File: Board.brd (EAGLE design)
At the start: 55.9 x 46.7 mm, 29 parts, among them Q1 N-MOS-FET, Q2 N-MOS-FET, Q3 N-MOS-FET, U2 STM32F07

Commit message: rev 2 preliminary, added power LED, power switch, necessary MCU pullups/downs and fets for the RGB
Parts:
- removed BARREL1: (no value), pinhead:1X02
- added PWR-SWITCH: (no value), pinhead:1X02
- C2: value 10uF -> 47uF; device rcl:C0805 -> rcl:C0603
- C3, C4: device rcl:C0805 -> rcl:C0603
- R1, R2, R3, R4, R5: device rcl:R0805 -> rcl:R0603
- R11, R12, R9: value 250 -> 250r; device rcl:R0805 -> rcl:R0603
- R6: value 250 -> 200; device rcl:R0805 -> rcl:R0603
- R7: value 300 -> 200; device rcl:R0805 -> rcl:R0603
- moved SWITCH 7.62 mm to (3.81, 29.2)
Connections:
- net N$1: now also PWR-SWITCH.2; no longer SWITCH.2
- net VBAT: now also SWITCH.2; no longer BARREL1.2
- net VIN: now also PWR-SWITCH.1; no longer BARREL1.1
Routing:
- net GND: vias 42 -> 43
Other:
- board text added: "B"
- board text added: "Designed By Michael Yablonovitch May 8 2018"
- board text added: "G"
- board text added: "MFLB Power Adapter - Rev.2"
- board text added: "R"
- board text removed: "MFLB Power Adapter - Rev.2 Designed By Michael Yablonovitch May 8 2018"

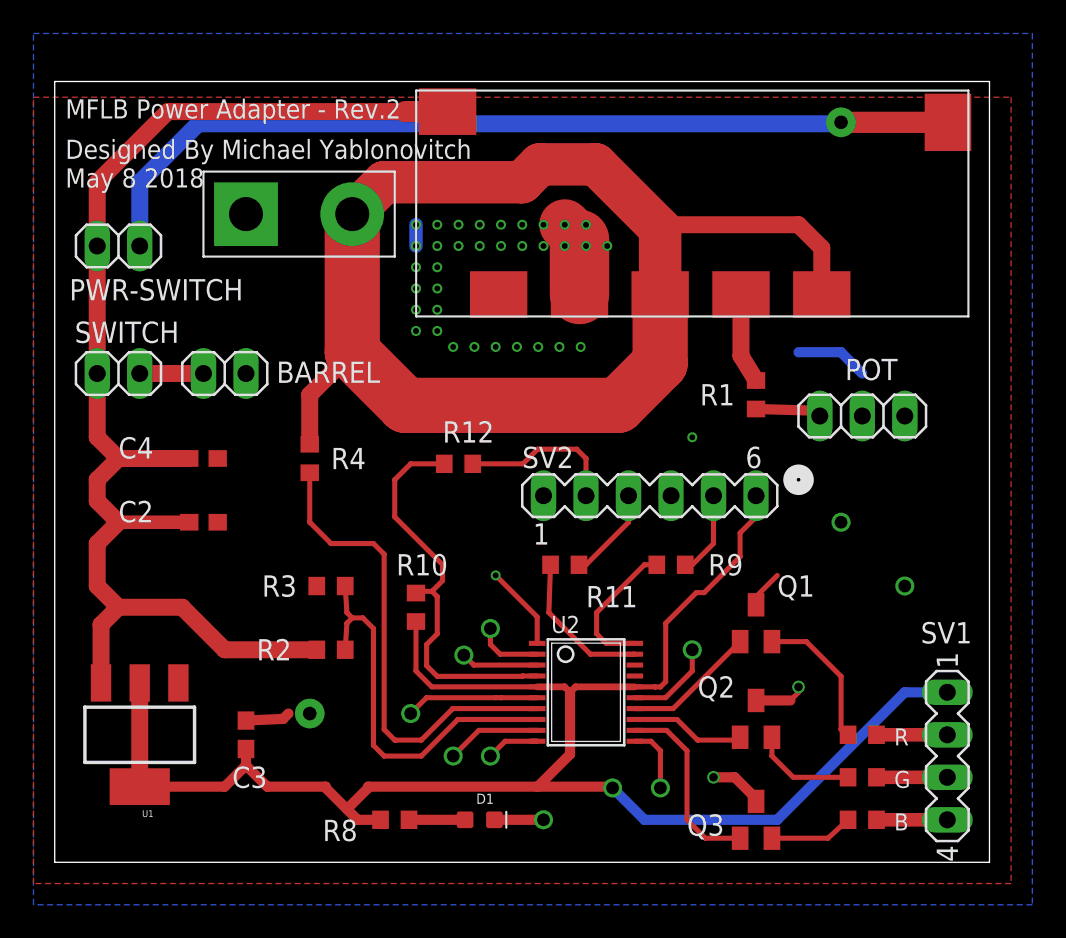
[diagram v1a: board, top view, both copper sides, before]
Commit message: switched n-mos to p-mos for common cathode RGBs
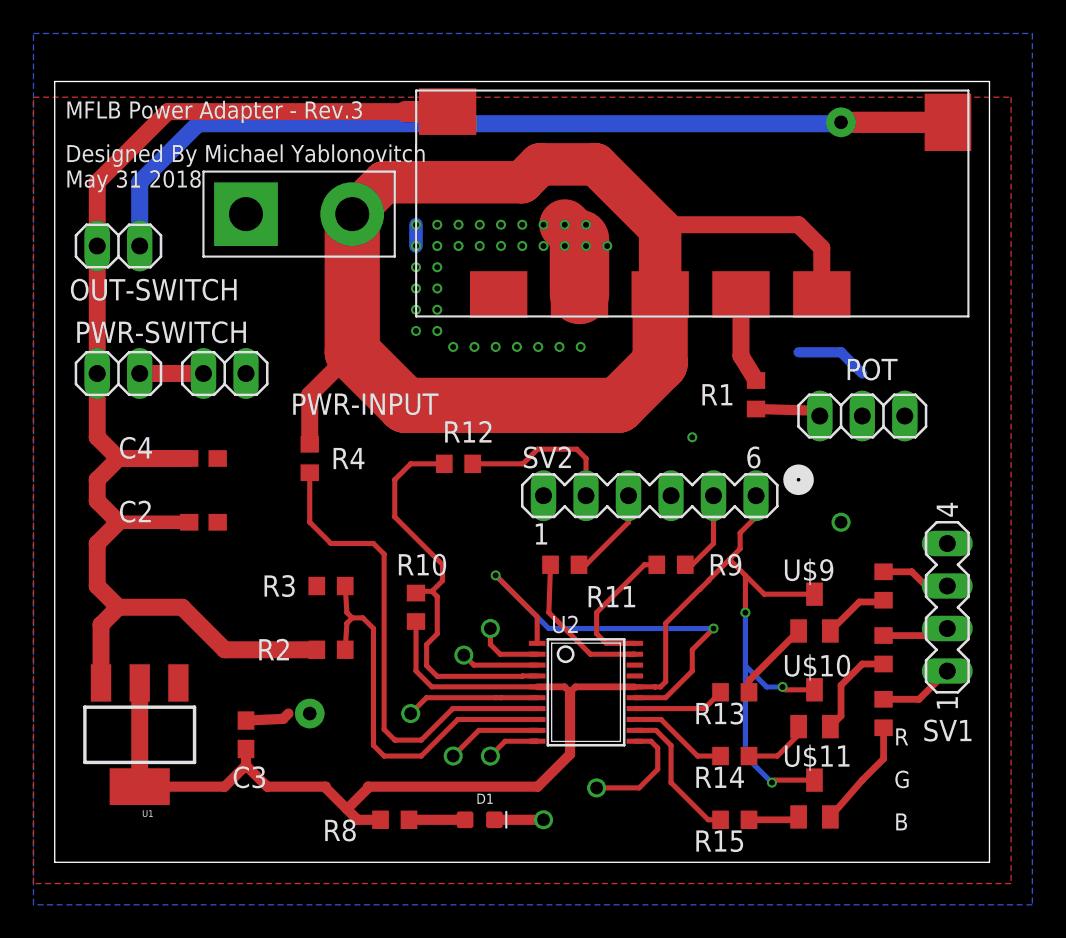
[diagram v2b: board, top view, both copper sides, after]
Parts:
- removed Q1, Q2, Q3: N-MOS-FET, YabzLib:SOT23
- removed SWITCH: (no value), pinhead:1X02
- added OUT-SWITCH: (no value), pinhead:1X02
- added R13, R14, R15: 250, rcl:R0603
- added U$10, U$11, U$9: P-MOS-FET, YabzLib:SOT23
- moved R5 8.98 mm to (49.5, 16.5), turned to 90 degrees
- moved SV1 8.89 mm to (53.3, 15.2), turned to 90 degrees
- moved R6 7.73 mm to (49.5, 12.7), turned to 90 degrees
- moved PWR-SWITCH 7.62 mm to (3.81, 29.2)
- moved R7 6.48 mm to (49.5, 8.89), turned to 90 degrees
- renumbered BARREL to PWR-INPUT
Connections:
- new net N$6: R7.2, SV1.1
- new net N$7: R13.1, U$9.B
- new net N$8: R14.1, U$10.B
- net +3V3: now also U$10.E, U$11.E, U$9.E; no longer SV1.1
- net GND: now also SV1.4; no longer Q1.E, Q2.E, Q3.E
- net LED-B: now also R15.2; no longer Q3.B
- net LED-G: now also R14.2; no longer Q2.B
- net LED-R: now also R13.2; no longer Q1.B
- net N$1: now also OUT-SWITCH.2; no longer PWR-SWITCH.2
- net N$11: now also R15.1, U$11.B; no longer R6.1, SV1.3
- net N$12: now also R5.1, U$9.C; no longer R7.1, SV1.4
- net N$13: now also R6.1, U$10.C; no longer Q2.C, R6.2
- net N$15: now also R7.1, U$11.C; no longer Q1.C, R5.2
- net N$2: now also R5.2, SV1.3; no longer R5.1, SV1.2
- net N$5: now also R6.2, SV1.2; no longer Q3.C, R7.2
- net VBAT: now also PWR-SWITCH.2; no longer SWITCH.2
- net VIN: now also OUT-SWITCH.1; no longer SWITCH.1
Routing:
- net GND: track 34.9 -> 42.4 mm, vias 43 -> 40
- net N$7: track 0.00 -> 4.89 mm
- net N$6: track 0.00 -> 4.51 mm
- net N$8: track 0.00 -> 3.98 mm
- net PA5: track 3.98 -> 6.92 mm
- net LED-B: track 11.4 -> 8.64 mm
- net LED-R: track 7.95 -> 5.53 mm
- net +3V3: track 102.7 -> 100.3 mm, vias 1 -> 3
- net N$15: track 8.69 -> 6.57 mm
- net N$11: track 4.23 -> 3.03 mm
- net LED-G: track 6.87 -> 6.03 mm
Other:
- board text added: "Designed By Michael Yablonovitch May 31 2018"
- board text added: "MFLB Power Adapter - Rev.3"
- board text removed: "Designed By Michael Yablonovitch May 8 2018"
- board text removed: "MFLB Power Adapter - Rev.2"
